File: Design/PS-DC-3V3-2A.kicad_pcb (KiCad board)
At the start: 2 copper layers, 24.1 x 13.7 mm, 13 parts, among them J1 Conn_01x02, J2 Conn_01x06, U1 MAX17643

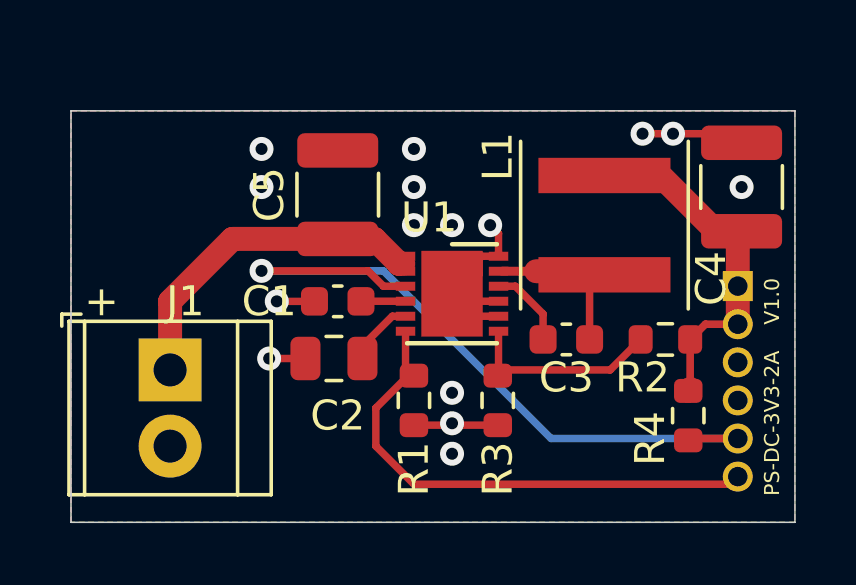
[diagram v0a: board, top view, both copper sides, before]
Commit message: Add led to the board
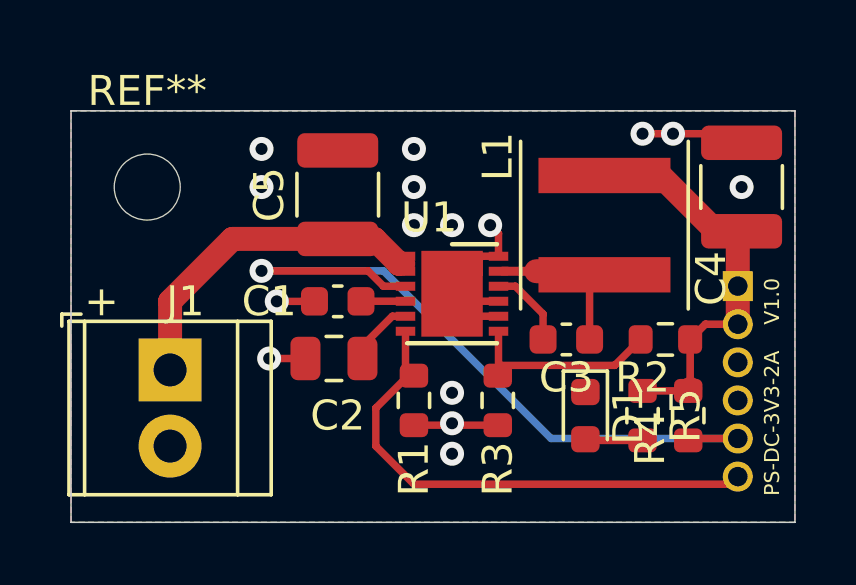
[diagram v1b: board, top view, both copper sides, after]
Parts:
- added D1: LED_Green, LED_SMD:LED_0603_1608Metric, F.Cu at (153.0, 104.1)
- added R5: 65R, Resistor_SMD:R_0603_1608Metric, F.Cu at (154.9, 104.1)
- added REF**: MountingHole_2.2mm_M2, MountingHole:MountingHole_2.2mm_M2, F.Cu at (138.4, 96.5)
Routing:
- net Net-(D1-Pad2): track 0.00 -> 1.92 mm
- net Vout: track 12.9 -> 14.4 mm
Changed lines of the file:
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@@
     (thickness 1.6)
     (drawings 13)
-    (tracks 94)
+    (tracks 98)
     (zones 0)
-    (modules 13)
-    (nets 11)
+    (modules 16)
+    (nets 12)
   )
   (page A4)
@@
   (net 9 \Reset)
   (net 10 SYNC)
+  (net 11 "Net-(D1-Pad2)")
   (net_class Default "This is the default net class."
     (clearance 0.2)
@@
     (add_net "Net-(C3-Pad1)")
     (add_net "Net-(C3-Pad2)")
+    (add_net "Net-(D1-Pad2)")
     (add_net "Net-(R2-Pad2)")
     (add_net SYNC)
@@
     (uvia_drill 0.1)
     (add_net Vout)
+  )
+  (module Resistor_SMD:R_0603_1608Metric (layer F.Cu)
+    (at 154.94 104.14 270)
+    (descr "Resistor SMD 0603 (1608 Metric), square (rectangular) end terminal, IPC_7351 nominal, (Body size source: IPC-SM-782 page 72, https://www.pcb-3d.com/wordpress/wp-content/uploads/ipc-sm-782a_amendment_1_and_2.pdf), generated with kicad-footprint-generator")
+    (tags resistor)
+    (attr smd)
+    (fp_text reference R5 (at 0 -1.43 90) (layer F.SilkS)
+      (effects (font (size 1 1) (thickness 0.15)))
+    )
+    (fp_text value 65R (at 0 1.43 90) (layer F.Fab)
+      (effects (font (size 1 1) (thickness 0.15)))
+    )
+    (fp_text user %R (at 0 0 90) (layer F.Fab)
+      (effects (font (size 0.4 0.4) (thickness 0.06)))
+    )
+    (fp_line (start -0.8 0.4125) (end -0.8 -0.4125) (layer F.Fab) (width 0.1))
+    (fp_line (start -0.8 -0.4125) (end 0.8 -0.4125) (layer F.Fab) (width 0.1))
+    (fp_line (start 0.8 -0.4125) (end 0.8 0.4125) (layer F.Fab) (width 0.1))
+    (fp_line (start 0.8 0.4125) (end -0.8 0.4125) (layer F.Fab) (width 0.1))
+    (fp_line (start -0.237258 -0.5225) (end 0.237258 -0.5225) (layer F.SilkS) (width 0.12))
+    (fp_line (start -0.237258 0.5225) (end 0.237258 0.5225) (layer F.SilkS) (width 0.12))
+    (fp_line (start -1.48 0.73) (end -1.48 -0.73) (layer F.CrtYd) (width 0.05))
+    (fp_line (start -1.48 -0.73) (end 1.48 -0.73) (layer F.CrtYd) (width 0.05))
+    (fp_line (start 1.48 -0.73) (end 1.48 0.73) (layer F.CrtYd) (width 0.05))
+    (fp_line (start 1.48 0.73) (end -1.48 0.73) (layer F.CrtYd) (width 0.05))
+    (pad 2 smd roundrect (at 0.825 0 270) (size 0.8 0.95) (layers F.Cu F.Paste F.Mask) (roundrect_rratio 0.25)
+      (net 11 "Net-(D1-Pad2)"))
+    (pad 1 smd roundrect (at -0.825 0 270) (size 0.8 0.95) (layers F.Cu F.Paste F.Mask) (roundrect_rratio 0.25)
+      (net 6 Vout))
+    (model ${KISYS3DMOD}/Resistor_SMD.3dshapes/R_0603_1608Metric.wrl
+      (at (xyz 0 0 0))
+      (scale (xyz 1 1 1))
+      (rotate (xyz 0 0 0))
+    )
+  )
+  (module LED_SMD:LED_0603_1608Metric (layer F.Cu)
+    (at 153.035 104.14 270)
+    (descr "LED SMD 0603 (1608 Metric), square (rectangular) end terminal, IPC_7351 nominal, (Body size source: http://www.tortai-tech.com/upload/download/2011102023233369053.pdf), generated with kicad-footprint-generator")
+    (tags LED)
+    (attr smd)
+    (fp_text reference D1 (at 0 -1.43 90) (layer F.SilkS)
+      (effects (font (size 1 1) (thickness 0.15)))
+    )
+    (fp_text value LED_Green (at 0 1.43 90) (layer F.Fab)
+      (effects (font (size 1 1) (thickness 0.15)))
+    )
+    (fp_text user %R (at 0 0 90) (layer F.Fab)
+      (effects (font (size 0.4 0.4) (thickness 0.06)))
+    )
+    (fp_line (start 0.8 -0.4) (end -0.5 -0.4) (layer F.Fab) (width 0.1))
+    (fp_line (start -0.5 -0.4) (end -0.8 -0.1) (layer F.Fab) (width 0.1))
+    (fp_line (start -0.8 -0.1) (end -0.8 0.4) (layer F.Fab) (width 0.1))
+    (fp_line (start -0.8 0.4) (end 0.8 0.4) (layer F.Fab) (width 0.1))
+    (fp_line (start 0.8 0.4) (end 0.8 -0.4) (layer F.Fab) (width 0.1))
+    (fp_line (start 0.8 -0.735) (end -1.485 -0.735) (layer F.SilkS) (width 0.12))
+    (fp_line (start -1.485 -0.735) (end -1.485 0.735) (layer F.SilkS) (width 0.12))
+    (fp_line (start -1.485 0.735) (end 0.8 0.735) (layer F.SilkS) (width 0.12))
+    (fp_line (start -1.48 0.73) (end -1.48 -0.73) (layer F.CrtYd) (width 0.05))
+    (fp_line (start -1.48 -0.73) (end 1.48 -0.73) (layer F.CrtYd) (width 0.05))
+    (fp_line (start 1.48 -0.73) (end 1.48 0.73) (layer F.CrtYd) (width 0.05))
+    (fp_line (start 1.48 0.73) (end -1.48 0.73) (layer F.CrtYd) (width 0.05))
+    (pad 2 smd roundrect (at 0.7875 0 270) (size 0.875 0.95) (layers F.Cu F.Paste F.Mask) (roundrect_rratio 0.25)
+      (net 11 "Net-(D1-Pad2)"))
+    (pad 1 smd roundrect (at -0.7875 0 270) (size 0.875 0.95) (layers F.Cu F.Paste F.Mask) (roundrect_rratio 0.25)
+      (net 1 GND))
+    (model ${KISYS3DMOD}/LED_SMD.3dshapes/LED_0603_1608Metric.wrl
+      (at (xyz 0 0 0))
+      (scale (xyz 1 1 1))
+      (rotate (xyz 0 0 0))
+    )
+  )
+  (module MountingHole:MountingHole_2.2mm_M2 locked (layer F.Cu)
+    (at 138.43 96.52)
+    (descr "Mounting Hole 2.2mm, no annular, M2")
+    (tags "mounting hole 2.2mm no annular m2")
+    (attr virtual)
+    (fp_text reference REF** (at 0 -3.2) (layer F.SilkS)
+      (effects (font (size 1 1) (thickness 0.15)))
+    )
+    (fp_text value MountingHole_2.2mm_M2 (at 0 3.2) (layer F.Fab)
+      (effects (font (size 1 1) (thickness 0.15)))
+    )
+    (fp_circle (center 0 0) (end 2.45 0) (layer F.CrtYd) (width 0.05))
+    (fp_circle (center 0 0) (end 2.2 0) (layer Cmts.User) (width 0.15))
+    (fp_text user %R (at 0.3 0) (layer F.Fab)
+      (effects (font (size 1 1) (thickness 0.15)))
+    )
+    (pad 1 np_thru_hole circle (at 0 0) (size 2.2 2.2) (drill 2.2) (layers *.Cu *.Mask))
   )
   (module Coilcraft_inductor_SMD:L_Coilcraft_XAL5050-682 (layer F.Cu)
@@
   (segment (start 156.527 103.252) (end 156.464 103.315) (width 0.8) (layer F.Cu) (net 6))
   (segment (start 156.527 101.6) (end 156.527 103.252) (width 0.254) (layer F.Cu) (net 6))
+  (segment (start 154.94 103.315) (end 156.464 103.315) (width 0.254) (layer F.Cu) (net 6))
   (segment (start 147.04 98.826) (end 147.04 99.326) (width 0.25) (layer F.Cu) (net 7))
   (segment (start 146.812 99.075999) (end 146.964999 99.075999) (width 0.8) (layer F.Cu) (net 7))
@@
   (segment (start 150.14 102.781) (end 150.114 102.807) (width 0.25) (layer F.Cu) (net 8))
   (segment (start 150.14 101.326) (end 150.14 102.781) (width 0.25) (layer F.Cu) (net 8))
-  (segment (start 153.861 102.616) (end 150.368 102.616) (width 0.25) (layer F.Cu) (net 8))
-  (segment (start 154.877 101.6) (end 153.861 102.616) (width 0.25) (layer F.Cu) (net 8))
   (segment (start 150.368 102.616) (end 150.368 102.87) (width 0.25) (layer F.Cu) (net 8))
+  (segment (start 150.2156 102.4636) (end 150.368 102.616) (width 0.25) (layer F.Cu) (net 8))
+  (segment (start 154.0134 102.4636) (end 150.2156 102.4636) (width 0.25) (layer F.Cu) (net 8))
+  (segment (start 154.877 101.6) (end 154.0134 102.4636) (width 0.25) (layer F.Cu) (net 8))
   (via (at 142.24 99.314) (size 0.8) (drill 0.4) (layers F.Cu B.Cu) (net 9))
   (segment (start 145.791834 99.314) (end 142.24 99.314) (width 0.25) (layer F.Cu) (net 9))
@@
   (segment (start 147.32 106.426) (end 146.05 105.156) (width 0.25) (layer F.Cu) (net 10))
   (segment (start 158.115 106.426) (end 147.32 106.426) (width 0.25) (layer F.Cu) (net 10))
+  (segment (start 153.0725 104.965) (end 153.035 104.9275) (width 0.25) (layer F.Cu) (net 11))
+  (segment (start 154.94 104.965) (end 153.0725 104.965) (width 0.25) (layer F.Cu) (net 11))
   (zone (net 1) (net_name GND) (layer B.Cu) (hatch edge 0.508)
     (connect_pads (clearance 0.254))
